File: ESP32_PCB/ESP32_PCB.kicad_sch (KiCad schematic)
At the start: 27 parts, among them J1 USB_C_Receptacle, J2 ESC1, J3 ESC2, J4 Conn_02x04_Counter_Clockwise, J5 LED, U2 H3LIS331DL, U3 AP2112K-3.3, U5 ESP32-S3-MINI-1U

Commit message: Update LED footprint
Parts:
- J5: footprint (none) -> ESC_Connectors:2_Pin
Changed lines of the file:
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@@
 			)
 		)
-		(property "Footprint" ""
+		(property "Footprint" "ESC_Connectors:2_Pin"
 			(at 30.48 67.31 0)
 			(effects

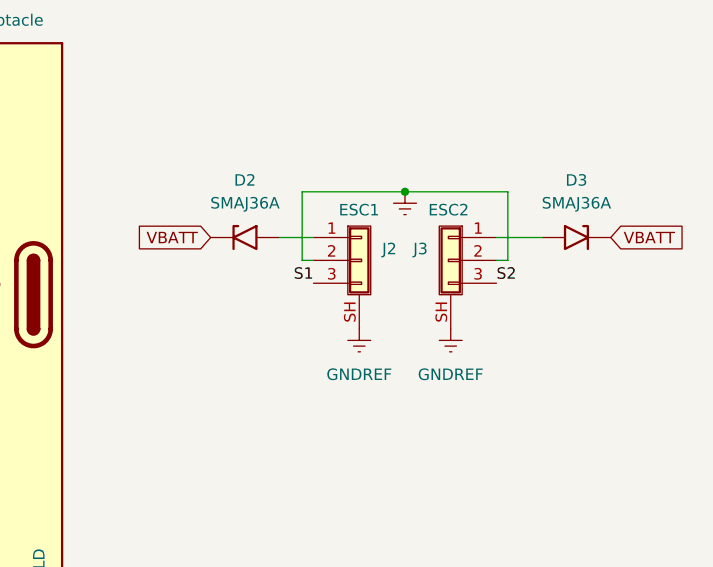
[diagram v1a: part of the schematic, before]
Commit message: Remove J2 and J3's SH pins
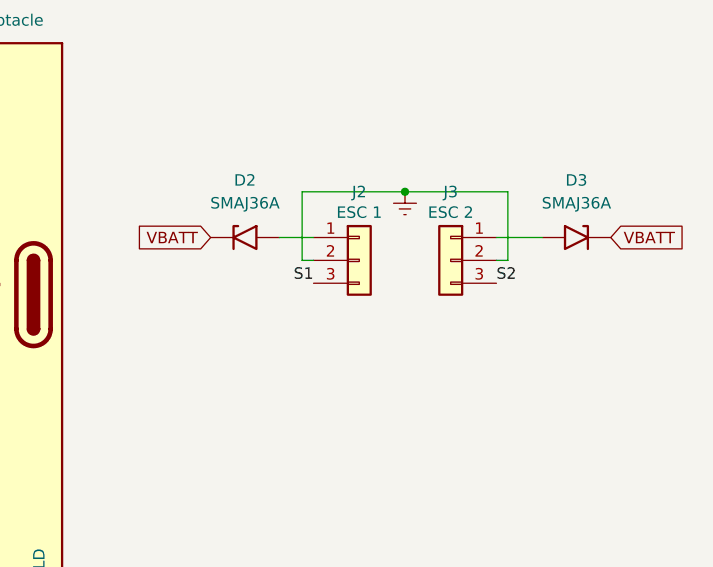
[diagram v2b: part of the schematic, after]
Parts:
- removed J2: ESC1, ESC_Connectors:3_Pin, symbol Connector_Generic_Shielded:Conn_01x03_Shielded
- removed J3: ESC2, ESC_Connectors:3_Pin, symbol Connector_Generic_Shielded:Conn_01x03_Shielded
- added J2: ESC 1, ESC_Connectors:3_Pin, symbol Connector_Generic:Conn_01x03
- added J3: ESC 2, ESC_Connectors:3_Pin, symbol Connector_Generic:Conn_01x03
- J4: value Conn_02x04_Counter_Clockwise -> EN & Boot Switches
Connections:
- net GNDREF: now also J2.2 (Pin_2), J3.2 (Pin_2)
- net S1: now also J2.3 (Pin_3)
- net S2: now also J3.3 (Pin_3)
- net at D3.2 (A2): now also J3.1 (Pin_1)
- net at D2.2 (A2): now also J2.1 (Pin_1)
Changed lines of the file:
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@@
 	)
 	(symbol
+		(lib_id "Connector_Generic:Conn_01x03")
+		(at 242.57 49.53 0)
+		(unit 1)
+		(exclude_from_sim no)
+		(in_bom yes)
+		(on_board yes)
+		(dnp no)
+		(property "Reference" "J2"
+			(at 242.57 42.672 0)
+			(effects
+				(font
+					(size 1.27 1.27)
+				)
+				(justify bottom)
+			)
+		)
+		(property "Value" "ESC 1"
+			(at 242.57 44.958 0)
+			(effects
+				(font
+					(size 1.27 1.27)
+				)
+				(justify bottom)
+			)
+		)
+		(property "Footprint" "ESC_Connectors:3_Pin"
+			(at 242.57 49.53 0)
+			(effects
+				(font
+					(size 1.27 1.27)
+				)
+				(hide yes)
+			)
+		)
+		(property "Datasheet" "~"
+			(at 242.57 49.53 0)
+			(effects
+				(font
+					(size 1.27 1.27)
+				)
+				(hide yes)
+			)
+		)
+		(property "Description" "Generic connector, single row, 01x03, script generated (kicad-library-utils/schlib/autogen/connector/)"
+			(at 242.57 49.53 0)
+			(effects
+				(font
+					(size 1.27 1.27)
+				)
+				(hide yes)
+			)
+		)
+		(pin "1"
+		)
+		(pin "2"
+		)
+		(pin "3"
+		)
+		(instances
+			(project ""
+				(path "/c820eee0-9a51-4601-b23c-3906ac354886"
+					(reference "J2")
+					(unit 1)
+				)
+			)
+		)
+	)
+	(symbol
 		(lib_id "power:GNDREF")
 		(at 29.21 133.35 0)
@@
 	)
 	(symbol
+		(lib_id "Connector_Generic:Conn_01x03")
+		(at 252.73 49.53 0)
+		(mirror y)
+		(unit 1)
+		(exclude_from_sim no)
+		(in_bom yes)
+		(on_board yes)
+		(dnp no)
+		(property "Reference" "J3"
+			(at 252.73 42.672 0)
+			(effects
+				(font
+					(size 1.27 1.27)
+				)
+				(justify bottom)
+			)
+		)
+		(property "Value" "ESC 2"
+			(at 252.73 44.958 0)
+			(effects
+				(font
+					(size 1.27 1.27)
+				)
+				(justify bottom)
+			)
+		)
+		(property "Footprint" "ESC_Connectors:3_Pin"
+			(at 252.73 49.53 0)
+			(effects
+				(font
+					(size 1.27 1.27)
+				)
+				(hide yes)
+			)
+		)
+		(property "Datasheet" "~"
+			(at 252.73 49.53 0)
+			(effects
+				(font
+					(size 1.27 1.27)
+				)
+				(hide yes)
+			)
+		)
+		(property "Description" "Generic connector, single row, 01x03, script generated (kicad-library-utils/schlib/autogen/connector/)"
+			(at 252.73 49.53 0)
+			(effects
+				(font
+					(size 1.27 1.27)
+				)
+				(hide yes)
+			)
+		)
+		(pin "1"
+		)
+		(pin "2"
+		)
+		(pin "3"
+		)
+		(instances
+			(project "ESP32_PCB"
+				(path "/c820eee0-9a51-4601-b23c-3906ac354886"
+					(reference "J3")
+					(unit 1)
+				)
+			)
+		)
+	)
+	(symbol
 		(lib_id "Diode:BAT54CW")
 		(at 160.02 63.5 0)
@@
 	)
 	(symbol
-		(lib_id "power:GNDREF")
-		(at 252.73 57.15 0)
-		(unit 1)
-		(exclude_from_sim no)
-		(in_bom yes)
-		(on_board yes)
-		(dnp no)
-		(fields_autoplaced yes)
-		(property "Reference" "#PWR035"
-			(at 252.73 63.5 0)
-			(effects
-				(font
-					(size 1.27 1.27)
-				)
-				(hide yes)
-			)
-		)
-		(property "Value" "GNDREF"
-			(at 252.73 62.23 0)
-			(effects
-				(font
-					(size 1.27 1.27)
-				)
-			)
-		)
-		(property "Footprint" ""
-			(at 252.73 57.15 0)
-			(effects
-				(font
-					(size 1.27 1.27)
-				)
-				(hide yes)
-			)
-		)
-		(property "Datasheet" ""
-			(at 252.73 57.15 0)
-			(effects
-				(font
-					(size 1.27 1.27)
-				)
-				(hide yes)
-			)
-		)
-		(property "Description" "Power symbol creates a global label with name \"GNDREF\" , reference supply ground"
-			(at 252.73 57.15 0)
-			(effects
-				(font
-					(size 1.27 1.27)
-				)
-				(hide yes)
-			)
-		)
-		(pin "1"
-		)
-		(instances
-			(project ""
-				(path "/c820eee0-9a51-4601-b23c-3906ac354886"
-					(reference "#PWR035")
-					(unit 1)
-				)
-			)
-		)
-	)
-	(symbol
 		(lib_id "Device:C_Polarized_Small_US")
 		(at 82.55 186.69 270)
@@
 	)
 	(symbol
-		(lib_id "Connector_Generic_Shielded:Conn_01x03_Shielded")
-		(at 242.57 49.53 0)
-		(unit 1)
-		(exclude_from_sim no)
-		(in_bom yes)
-		(on_board yes)
-		(dnp no)
-		(property "Reference" "J2"
-			(at 245.11 48.2599 0)
-			(effects
-				(font
-					(size 1.27 1.27)
-				)
-				(justify left)
-			)
-		)
-		(property "Value" "ESC1"
-			(at 240.284 43.942 0)
-			(effects
-				(font
-					(size 1.27 1.27)
-				)
-				(justify left)
-			)
-		)
-		(property "Footprint" "ESC_Connectors:3_Pin"
-			(at 242.57 49.53 0)
-			(effects
-				(font
-					(size 1.27 1.27)
-				)
-				(hide yes)
-			)
-		)
-		(property "Datasheet" "~"
-			(at 242.57 49.53 0)
-			(effects
-				(font
-					(size 1.27 1.27)
-				)
-				(hide yes)
-			)
-		)
-		(property "Description" "Generic shielded connector, single row, 01x03, script generated (kicad-library-utils/schlib/autogen/connector/)"
-			(at 242.57 49.53 0)
-			(effects
-				(font
-					(size 1.27 1.27)
-				)
-				(hide yes)
-			)
-		)
-		(pin "3"
-		)
-		(pin "SH"
-		)
-		(pin "2"
-		)
-		(pin "1"
-		)
-		(instances
-			(project ""
-				(path "/c820eee0-9a51-4601-b23c-3906ac354886"
-					(reference "J2")
-					(unit 1)
-				)
-			)
-		)
-	)
-	(symbol
 		(lib_id "power:GNDREF")
 		(at 44.45 43.18 0)
@@
 	)
 	(symbol
-		(lib_id "Connector_Generic_Shielded:Conn_01x03_Shielded")
-		(at 252.73 49.53 0)
-		(mirror y)
-		(unit 1)
-		(exclude_from_sim no)
-		(in_bom yes)
-		(on_board yes)
-		(dnp no)
-		(property "Reference" "J3"
-			(at 250.19 48.2599 0)
-			(effects
-				(font
-					(size 1.27 1.27)
-				)
-				(justify left)
-			)
-		)
-		(property "Value" "ESC2"
-			(at 254.762 43.942 0)
-			(effects
-				(font
-					(size 1.27 1.27)
-				)
-				(justify left)
-			)
-		)
-		(property "Footprint" "ESC_Connectors:3_Pin"
-			(at 252.73 49.53 0)
-			(effects
-				(font
-					(size 1.27 1.27)
-				)
-				(hide yes)
-			)
-		)
-		(property "Datasheet" "~"
-			(at 252.73 49.53 0)
-			(effects
-				(font
-					(size 1.27 1.27)
-				)
-				(hide yes)
-			)
-		)
-		(property "Description" "Generic shielded connector, single row, 01x03, script generated (kicad-library-utils/schlib/autogen/connector/)"
-			(at 252.73 49.53 0)
-			(effects
-				(font
-					(size 1.27 1.27)
-				)
-				(hide yes)
-			)
-		)
-		(pin "3"
-		)
-		(pin "SH"
-		)
-		(pin "2"
-		)
-		(pin "1"
-		)
-		(instances
-			(project "ESP32_PCB"
-				(path "/c820eee0-9a51-4601-b23c-3906ac354886"
-					(reference "J3")
-					(unit 1)
-				)
-			)
-		)
-	)
-	(symbol
 		(lib_id "power:GNDREF")
 		(at 167.64 72.39 90)
@@
 	(symbol
 		(lib_id "power:GNDREF")
-		(at 242.57 57.15 0)
-		(unit 1)
-		(exclude_from_sim no)
-		(in_bom yes)
-		(on_board yes)
-		(dnp no)
-		(fields_autoplaced yes)
-		(property "Reference" "#PWR034"
-			(at 242.57 63.5 0)
-			(effects
-				(font
-					(size 1.27 1.27)
-				)
-				(hide yes)
-			)
-		)
-		(property "Value" "GNDREF"
-			(at 242.57 62.23 0)
-			(effects
-				(font
-					(size 1.27 1.27)
-				)
-			)
-		)
-		(property "Footprint" ""
-			(at 242.57 57.15 0)
-			(effects
-				(font
-					(size 1.27 1.27)
-				)
-				(hide yes)
-			)
-		)
-		(property "Datasheet" ""
-			(at 242.57 57.15 0)
-			(effects
-				(font
-					(size 1.27 1.27)
-				)
-				(hide yes)
-			)
-		)
-		(property "Description" "Power symbol creates a global label with name \"GNDREF\" , reference supply ground"
-			(at 242.57 57.15 0)
-			(effects
-				(font
-					(size 1.27 1.27)
-				)
-				(hide yes)
-			)
-		)
-		(pin "1"
-		)
-		(instances
-			(project ""
-				(path "/c820eee0-9a51-4601-b23c-3906ac354886"
-					(reference "#PWR034")
-					(unit 1)
-				)
-			)
-		)
-	)
-	(symbol
-		(lib_id "power:GNDREF")
 		(at 106.68 91.44 0)
 		(unit 1)
@@
 			)
 		)
-		(property "Value" "Conn_02x04_Counter_Clockwise"
+		(property "Value" "EN & Boot Switches"
 			(at 36.83 30.48 0)
 			(effects

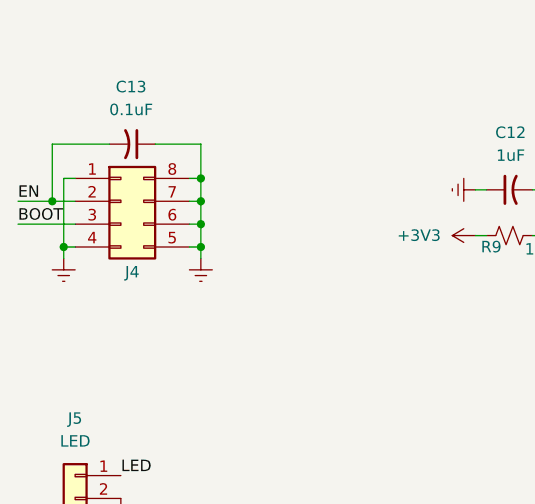
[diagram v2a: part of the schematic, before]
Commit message: Finish EN & Boot header pins layout
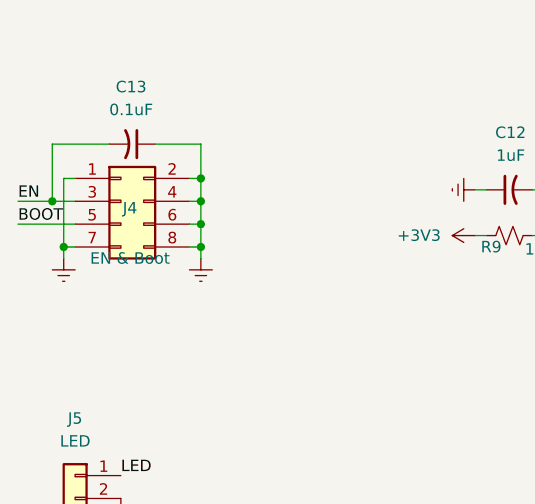
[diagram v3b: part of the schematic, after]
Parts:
- removed J4: EN & Boot Switches, Connector_PinSocket_1.00mm:PinSocket_2x04_P1.00mm_Vertical_SMD, symbol Connector_Generic:Conn_02x04_Counter_Clockwise
- added J4: EN & Boot, Connector_PinHeader_1.00mm:PinHeader_2x04_P1.00mm_Vertical, symbol Connector_Generic:Conn_02x04_Odd_Even
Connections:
- net BOOT: now also J4.5 (Pin_5)
- net EN: now also J4.3 (Pin_3)
- net GNDREF: now also J4.1 (Pin_1), J4.2 (Pin_2), J4.4 (Pin_4), J4.6 (Pin_6), J4.7 (Pin_7), J4.8 (Pin_8)
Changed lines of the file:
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@@
+	)
+	(symbol
+		(lib_id "Connector_Generic:Conn_02x04_Odd_Even")
+		(at 35.56 36.83 0)
+		(unit 1)
+		(exclude_from_sim no)
+		(in_bom yes)
+		(on_board yes)
+		(dnp no)
+		(property "Reference" "J4"
+			(at 36.576 37.592 0)
+			(effects
+				(font
+					(size 1.27 1.27)
+				)
+			)
+		)
+		(property "Value" "EN & Boot"
+			(at 36.576 43.18 0)
+			(effects
+				(font
+					(size 1.27 1.27)
+				)
+			)
+		)
+		(property "Footprint" "Connector_PinHeader_1.00mm:PinHeader_2x04_P1.00mm_Vertical"
+			(at 35.56 36.83 0)
+			(effects
+				(font
+					(size 1.27 1.27)
+				)
+				(hide yes)
+			)
+		)
+		(property "Datasheet" "~"
+			(at 35.56 36.83 0)
+			(effects
+				(font
+					(size 1.27 1.27)
+				)
+				(hide yes)
+			)
+		)
+		(property "Description" "Generic connector, double row, 02x04, odd/even pin numbering scheme (row 1 odd numbers, row 2 even numbers), script generated (kicad-library-utils/schlib/autogen/connector/)"
+			(at 35.56 36.83 0)
+			(effects
+				(font
+					(size 1.27 1.27)
+				)
+				(hide yes)
+			)
+		)
+		(pin "2"
+		)
+		(pin "4"
+		)
+		(pin "6"
+		)
+		(pin "8"
+		)
+		(pin "3"
+		)
+		(pin "5"
+		)
+		(pin "1"
+		)
+		(pin "7"
+		)
+		(instances
+			(project ""
+				(path "/c820eee0-9a51-4601-b23c-3906ac354886"
+					(reference "J4")
+					(unit 1)
+				)
+			)
+		)
 	)
 	(symbol
@@
 					(unit 1)
 				)
-			)
-		)
-	)
-	(symbol
-		(lib_id "Connector_Generic:Conn_02x04_Counter_Clockwise")
-		(at 35.56 36.83 0)
-		(unit 1)
-		(exclude_from_sim no)
-		(in_bom yes)
-		(on_board yes)
-		(dnp no)
-		(property "Reference" "J4"
-			(at 36.83 44.704 0)
-			(effects
-				(font
-					(size 1.27 1.27)
-				)
-			)
-		)
-		(property "Value" "EN & Boot Switches"
-			(at 36.83 30.48 0)
-			(effects
-				(font
-					(size 1.27 1.27)
-				)
-				(hide yes)
-			)
-		)
-		(property "Footprint" "Connector_PinSocket_1.00mm:PinSocket_2x04_P1.00mm_Vertical_SMD"
-			(at 35.56 36.83 0)
-			(effects
-				(font
-					(size 1.27 1.27)
-				)
-				(hide yes)
-			)
-		)
-		(property "Datasheet" "~"
-			(at 35.56 36.83 0)
-			(effects
-				(font
-					(size 1.27 1.27)
-				)
-				(hide yes)
-			)
-		)
-		(property "Description" "Generic connector, double row, 02x04, counter clockwise pin numbering scheme (similar to DIP package numbering), script generated (kicad-library-utils/schlib/autogen/connector/)"
-			(at 35.56 36.83 0)
-			(effects
-				(font
-					(size 1.27 1.27)
-				)
-				(hide yes)
-			)
-		)
-		(pin "8"
-		)
-		(pin "7"
-		)
-		(pin "4"
-		)
-		(pin "2"
-		)
-		(pin "1"
-		)
-		(pin "3"
-		)
-		(pin "5"
-		)
-		(pin "6"
-		)
-		(instances
-			(project ""
-				(path "/c820eee0-9a51-4601-b23c-3906ac354886"
-					(reference "J4")
-					(unit 1)
-				)

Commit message: Fix the size of the header pins
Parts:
- J4: footprint Connector_PinHeader_1.00mm:PinHeader_2x04_P1.00mm_Vertical -> Connector_PinHeader_2.54mm:PinHeader_2x04_P2.54mm_Vertical
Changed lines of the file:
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@@
 			)
 		)
-		(property "Footprint" "Connector_PinHeader_1.00mm:PinHeader_2x04_P1.00mm_Vertical"
+		(property "Footprint" "Connector_PinHeader_2.54mm:PinHeader_2x04_P2.54mm_Vertical"
 			(at 35.56 36.83 0)
 			(effects
